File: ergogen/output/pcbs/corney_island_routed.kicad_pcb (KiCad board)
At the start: 2 copper layers, 134.2 x 92.7 mm, 73 parts

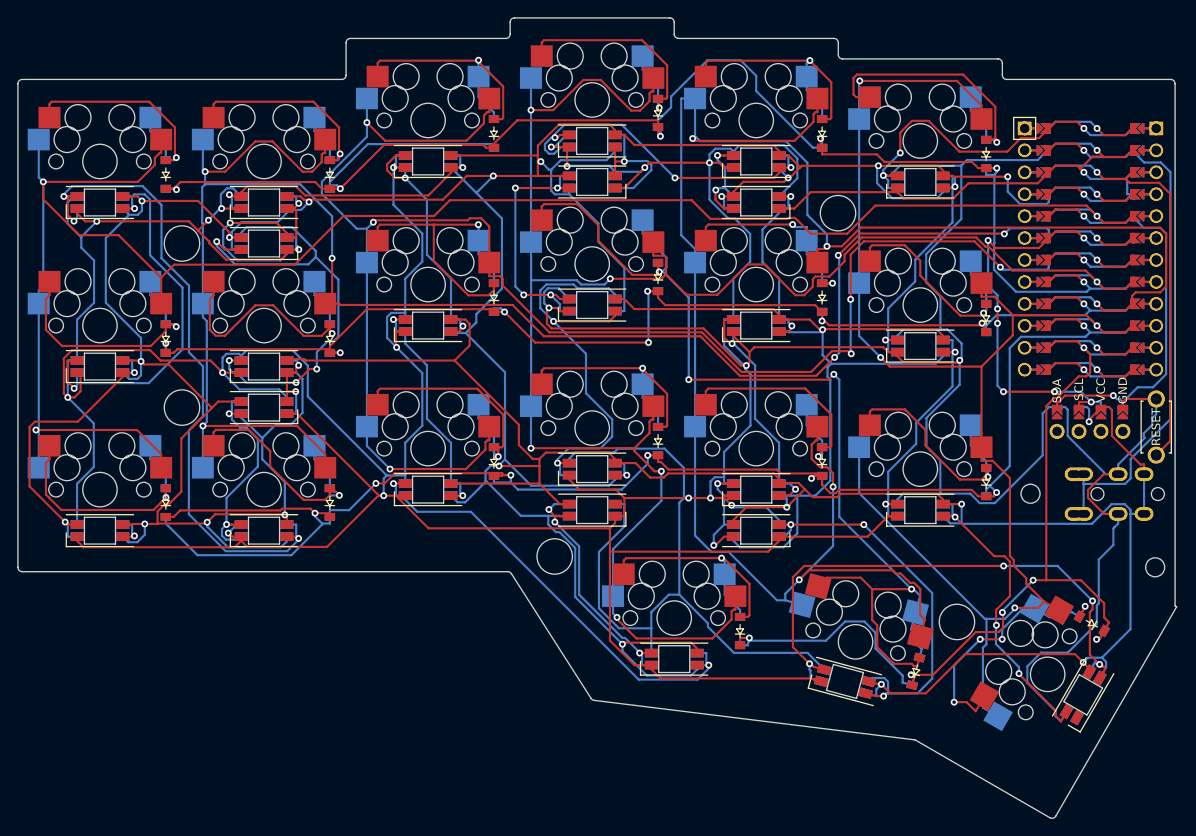
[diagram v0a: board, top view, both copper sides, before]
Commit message: Fix inner underglow LED position
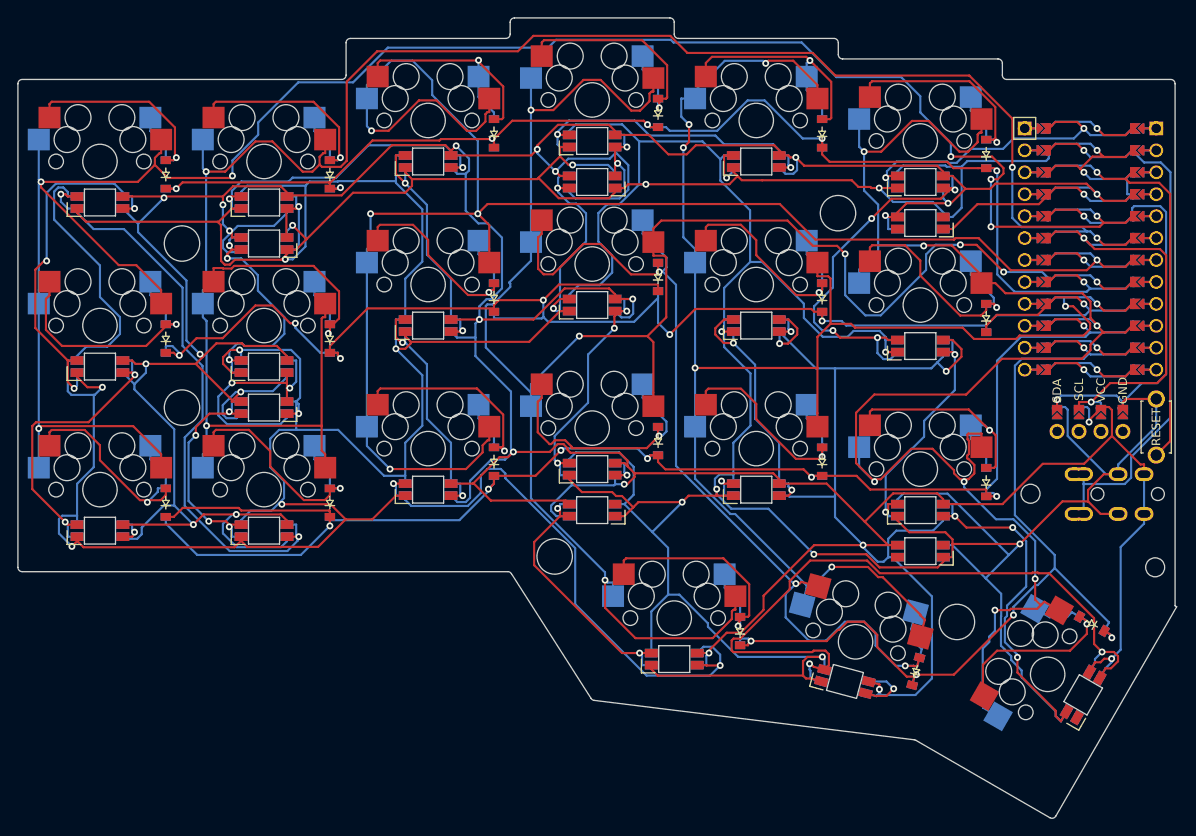
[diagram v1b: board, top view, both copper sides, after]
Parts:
- moved LED26 19.1 mm to (195.0, 107.1)
- moved LED27 19.1 mm to (195.0, 69.1)
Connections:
- LED26 pad 2: ULED_5 -> (no net)
- LED26 pad 4: LED_5 -> (no net)
- LED27 pad 2: ULED_6 -> (no net)
- LED27 pad 4: LED_7 -> (no net)
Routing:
- net VCC: track 789.2 -> 726.1 mm, vias 22 -> 26
- net LED_5: track 45.8 -> 6.91 mm, vias 3 -> 1
- net C4: track 227.2 -> 189.0 mm, vias 5 -> 7
- net R1: track 144.0 -> 176.8 mm, vias 8 -> 7
- net R0: track 180.2 -> 152.0 mm, vias 6 -> 7
- net LED_16: track 57.6 -> 29.9 mm, vias 4 -> 3
- net GND: track 897.2 -> 874.3 mm, vias 23 -> 21
- net LED_10: track 50.0 -> 28.8 mm, vias 2 -> 3
- net C0: track 222.1 -> 241.4 mm, vias 3 -> 7
- net LED_7: track 22.3 -> 3.97 mm, vias 2 -> 1
- net C5: track 175.9 -> 194.1 mm, vias 4 -> 7
- net LED_4: track 64.7 -> 81.7 mm, vias 4 -> 2
- net ULED_0: track 11.8 -> 28.2 mm
- net LED_1: track 30.1 -> 45.1 mm, vias 2 -> 4
- net ULED_1: track 27.7 -> 13.4 mm, vias 2 -> 1
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
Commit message: Overhaul outlines making use of intersect
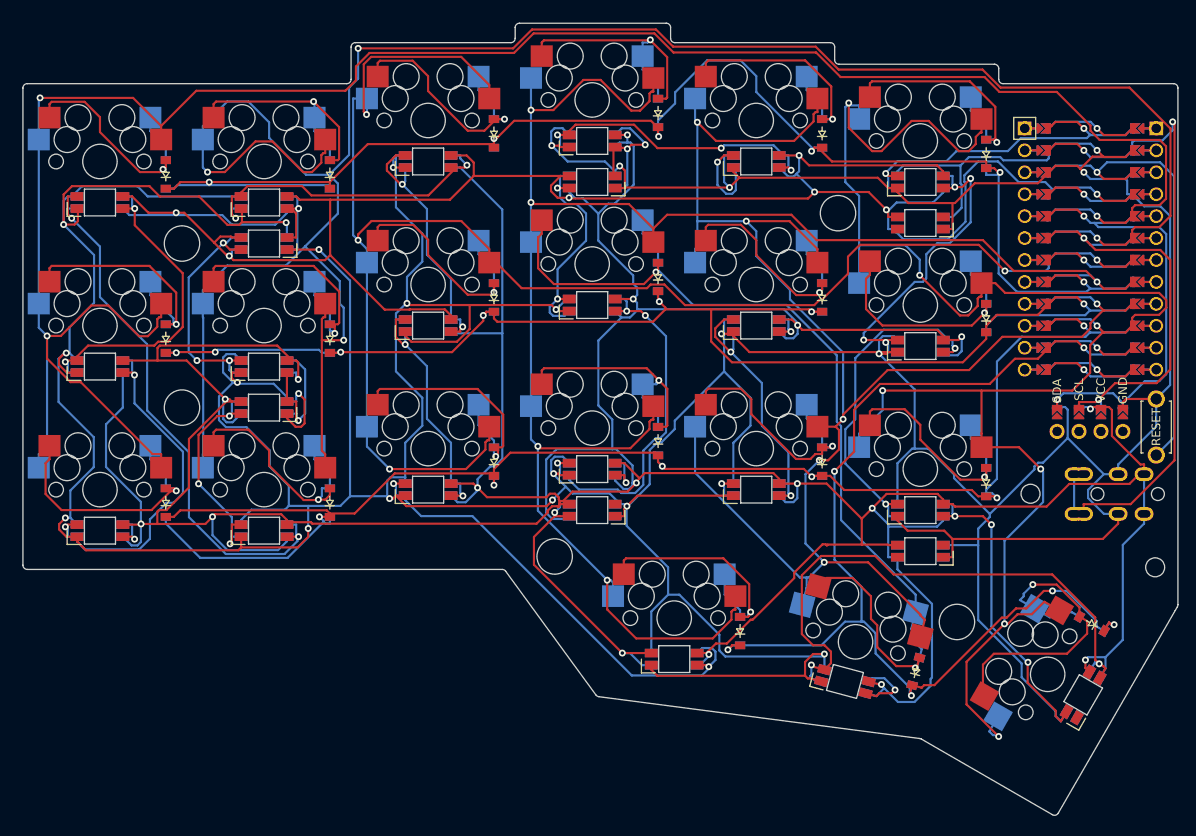
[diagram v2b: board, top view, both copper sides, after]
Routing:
- net VCC: track 726.1 -> 794.9 mm, vias 26 -> 23
- net C1: track 218.8 -> 267.9 mm
- net GND: track 874.3 -> 847.6 mm, vias 21 -> 24
- net R0: track 152.0 -> 175.9 mm, vias 7 -> 6
- net R3: track 109.8 -> 128.2 mm, vias 5 -> 6
- net C5: track 194.1 -> 210.5 mm
- net LED_4: track 81.7 -> 65.5 mm
- net C3: track 223.1 -> 207.5 mm, vias 7 -> 5
- net R1: track 176.8 -> 161.8 mm
- net LED_10: track 28.8 -> 42.4 mm
- net C2: track 203.7 -> 191.1 mm
- net data: track 66.6 -> 78.2 mm, vias 1 -> 2
- net LED_12: track 66.0 -> 54.6 mm
- net ULED_0: track 28.2 -> 17.5 mm, vias 2 -> 1
- net far_home: track 26.9 -> 37.5 mm
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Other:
- board size 134.2 x 92.7 mm -> 133.8 x 91.7 mm

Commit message: Change to relative measures for helper points
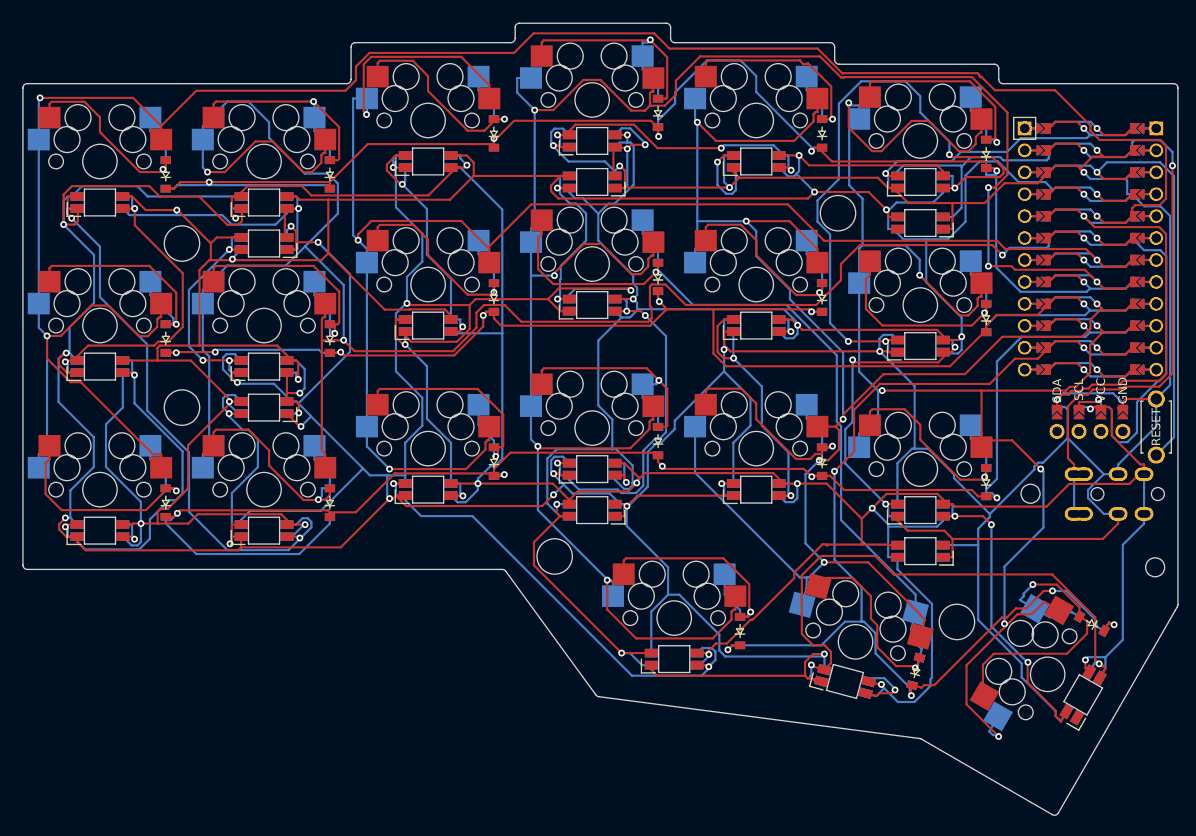
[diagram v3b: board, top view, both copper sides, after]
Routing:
- net LED_1: track 37.9 -> 75.4 mm
- net C1: track 267.9 -> 233.8 mm
- net C3: track 207.5 -> 237.9 mm, vias 5 -> 7
- net VCC: track 794.9 -> 772.4 mm, vias 23 -> 22
- net C5: track 210.5 -> 195.6 mm
- net SDA: track 52.7 -> 61.9 mm
- net data: track 78.2 -> 71.7 mm
- net GND: track 847.6 -> 851.1 mm, vias 24 -> 23
- net ULED_0: track 17.5 -> 14.3 mm, vias 1 -> 2
- net LED_18: track 65.9 -> 68.5 mm
- net LED_9: track 26.3 -> 24.0 mm
- net R1: track 161.8 -> 163.5 mm
- net LED_16: track 28.1 -> 26.4 mm
- net C2: track 191.1 -> 192.5 mm, vias 5 -> 4
- net SCL: track 48.6 -> 49.9 mm
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
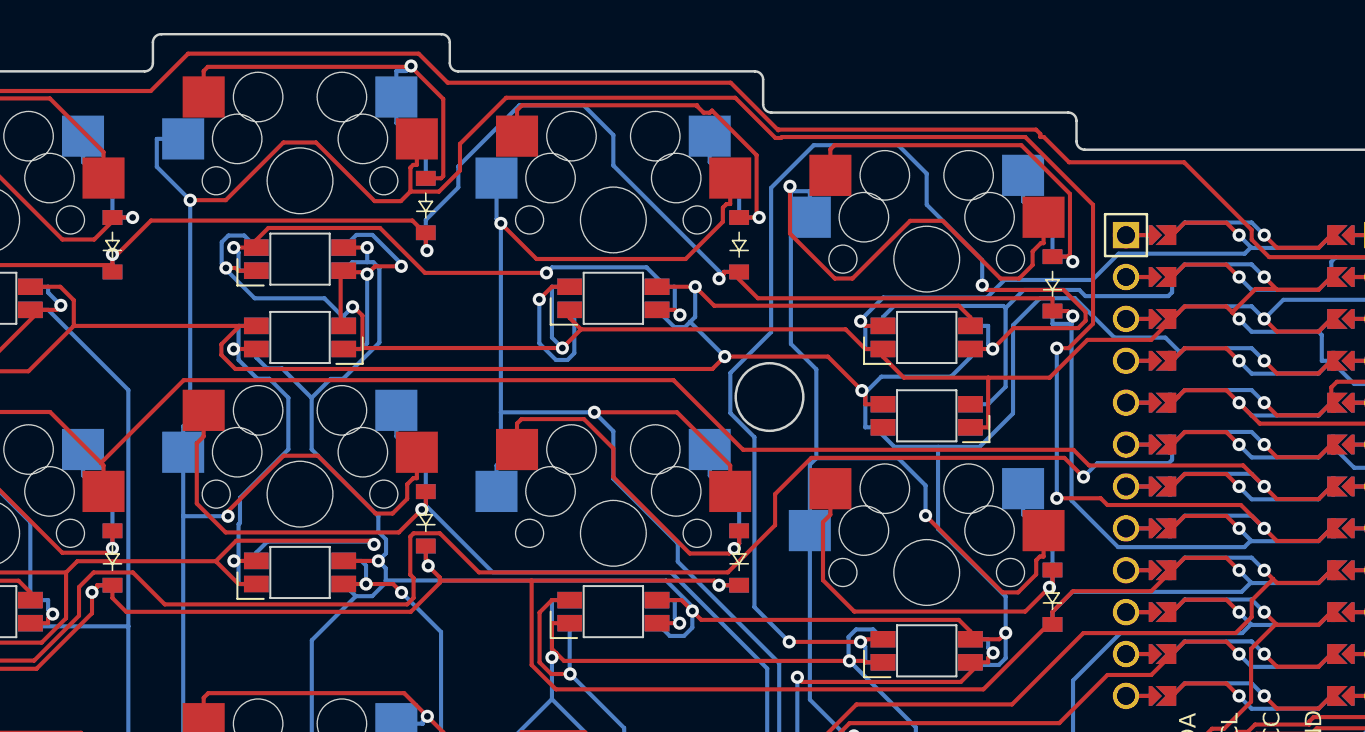
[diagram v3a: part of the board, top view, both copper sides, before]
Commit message: Add missing parametric measures
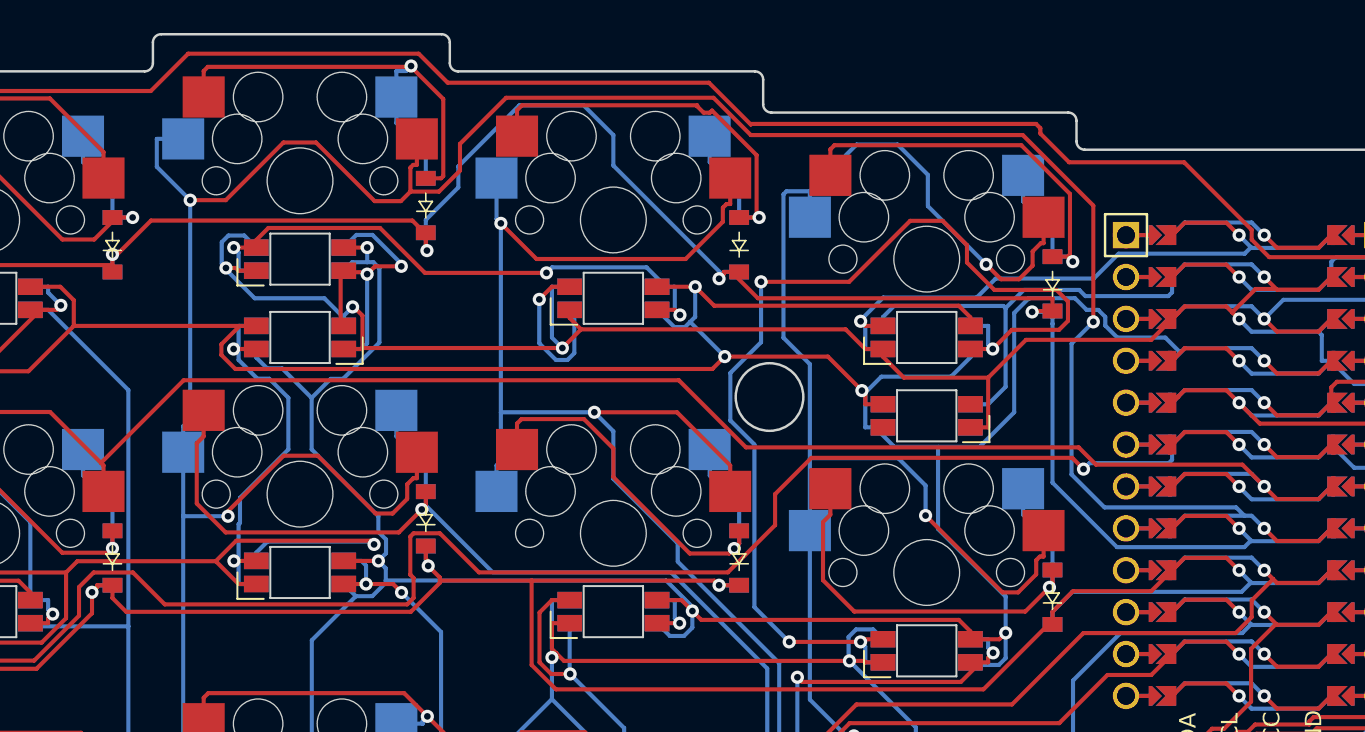
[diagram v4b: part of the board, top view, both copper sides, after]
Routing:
- net LED_1: track 75.4 -> 65.4 mm
- net C3: track 237.9 -> 233.8 mm, vias 7 -> 6
- net C5: track 195.6 -> 193.4 mm
- net VCC: track 772.4 -> 773.1 mm

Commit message: Refresh generated files.
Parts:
- D1, D10, D11, D12, D13, D14, D15, D16, D17, D18, D19, D2, D20, D21, D3, D4, D5, D6, D7, D8, D9: moved to B.Cu
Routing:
- net GND: track 851.1 -> 893.6 mm, vias 23 -> 25
- net LED_10: track 42.5 -> 84.3 mm, vias 3 -> 2
- net LED_1: track 65.4 -> 33.1 mm, vias 4 -> 3
- net C1: track 233.4 -> 258.5 mm, vias 4 -> 6
- net VCC: track 773.1 -> 752.5 mm, vias 22 -> 27
- net R1: track 163.5 -> 145.6 mm, vias 7 -> 6
- net R0: track 175.3 -> 159.8 mm, vias 6 -> 8
- net LED_8: track 35.8 -> 49.9 mm, vias 3 -> 5
- net far_home: track 37.5 -> 24.0 mm, vias 1 -> 2
- net middle_home: track 114.7 -> 101.6 mm, vias 2 -> 4
- net LED_4: track 65.5 -> 53.9 mm
- net SDA: track 61.9 -> 51.6 mm
- net LED_2: track 38.4 -> 29.0 mm, vias 3 -> 2
- net LED_14: track 29.6 -> 38.6 mm
- net LED_12: track 54.6 -> 62.4 mm
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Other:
- outline, holes or cut-outs redrawn
